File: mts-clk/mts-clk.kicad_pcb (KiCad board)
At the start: 2 copper layers, 70 x 63.6 mm, 71 parts, among them IC1 SCPHS-13.6+, J1 Input (SMA), J2 Output (SMA), J3 Output (SMA), J4 Power Conn., J5 S2B-PH-K-SLFSN, U1 TCP-2-10X, U2 LTC6433BIUF-15-TRPBF, U3 LTC6433BIUF-15-TRPBF, U4 OPA197xD

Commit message: layout for CLK
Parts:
- added G***: LOGO, posm-logo:posm-logo-footprint, F.Cu at (159.4, 132.3)
- moved C27 150.6 mm to (172.9, 121.6)
- moved R11 144.2 mm to (171.1, 125.0), turned to 180 degrees
- moved C28 142.7 mm to (171.2, 114.3)
- moved R12 140.4 mm to (170.2, 121.6), turned to 90 degrees
- moved J3 139.8 mm to (146.4, 131.9)
- moved C25 137.6 mm to (167.4, 101.9), turned to 180 degrees
- moved R13 137.2 mm to (170.2, 117.6), turned to 90 degrees
- moved C26 134.3 mm to (167.4, 99.4), turned to 180 degrees
- moved R14 131.9 mm to (167.7, 113.5)
- moved R16 128.7 mm to (163.4, 109.5), turned to -90 degrees
- moved TP4 127.9 mm to (167.3, 125.6)
- moved R15 127.2 mm to (165.6, 109.5), turned to -90 degrees
- moved L3 124.5 mm to (120.4, 125.2), turned to 180 degrees
- moved C21 121.4 mm to (126.7, 126.8), turned to 90 degrees
- moved TP3 121.1 mm to (164.1, 114.2), turned to 90 degrees
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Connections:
- IC1 pad 12: Net-(IC1-GROUND_10) -> GND
- IC1 pad 13: Net-(IC1-GROUND_10) -> GND
- IC1 pad 14: Net-(IC1-GROUND_10) -> GND
- J3 pad 3: (no net) -> GND
- J3 pad 4: (no net) -> GND
- J3 pad 5: (no net) -> GND
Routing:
- net PORT2: track 0.00 -> 15.1 mm
- net PORT1: track 0.00 -> 13.7 mm
- net 10MHz_EOM: track 0.00 -> 12.5 mm
- net PORT2_POST_amp: track 0.00 -> 10.4 mm
- net 10MHz_DEMOD: track 0.00 -> 10.1 mm
- net Net-(L3-Pad1): track 0.00 -> 7.86 mm
- net Net-(U3-FDBK): track 0.00 -> 7.84 mm, vias 0 -> 2
- net FDBK1: track 0.00 -> 7.59 mm
- net FDBK2: track 0.00 -> 7.30 mm
- net 10MHz_INPUT: track 0.00 -> 6.46 mm
- net Net-(L1-Pad1): track 0.00 -> 5.70 mm
- net PORT1_POST_amp: track 0.00 -> 5.51 mm
- net Net-(U2-IN): track 0.00 -> 5.46 mm
- net Net-(U3-IN): track 0.00 -> 5.01 mm
- net PORT2_post_phase: track 0.00 -> 4.93 mm
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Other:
- board size 70 x 63.6 mm -> 59.9 x 61.7 mm
- board text added: "mts-clk-v0"

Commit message: idek man
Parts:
- moved C32 6.32 mm to (126.8, 89.7), turned to 180 degrees
- moved C31 4.03 mm to (122.5, 90.1), turned to 0 degrees
- moved C27 2.05 mm to (172.9, 119.6)
- moved C14 0.91 mm to (119.6, 117.3)
- moved C29 0.91 mm to (119.3, 115.8)
- moved R14 0.60 mm to (167.2, 113.9), turned to 90 degrees
- moved C19 0.31 mm to (128.3, 117.3), turned to 90 degrees
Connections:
- J2 pad 3: (no net) -> GND
- J2 pad 4: (no net) -> GND
- J2 pad 5: (no net) -> GND
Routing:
- net TDIODE2: track 0.00 -> 46.9 mm, vias 0 -> 2
- net TDIODE1: track 0.00 -> 18.3 mm, vias 0 -> 2
- net GND: track 0.00 -> 15.8 mm, vias 0 -> 92
- net Net-(R15-Pad1): track 0.00 -> 12.6 mm, vias 0 -> 2
- net Net-(U4--): track 0.00 -> 7.04 mm
- net Net-(U4-+): track 0.00 -> 6.15 mm
- net V_FPGA_PWM: track 4.33 -> 9.18 mm
- net Net-(C27-Pad1): track 0.00 -> 4.60 mm
- net Net-(U3-NFILT): track 0.00 -> 1.91 mm
- net Net-(U3-IN): track 5.01 -> 5.67 mm
- net +5V: vias 0 -> 40
- net +15V: vias 0 -> 14
- added copper zone on F.Cu, net +15V
- added copper zone on In2.Cu, net +15V
- added copper zone on F.Cu, net +5V
- added copper zone on In2.Cu, net +5V
- added copper zone on B.Cu, net GND
- added copper zone on F.Cu, net GND
- added copper zone on In1.Cu, net GND
- added copper zone on F.Cu, net V_CONTROL
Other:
- board size 59.9 x 61.7 mm -> 60.2 x 61.7 mm
- copper layers 2 -> 4

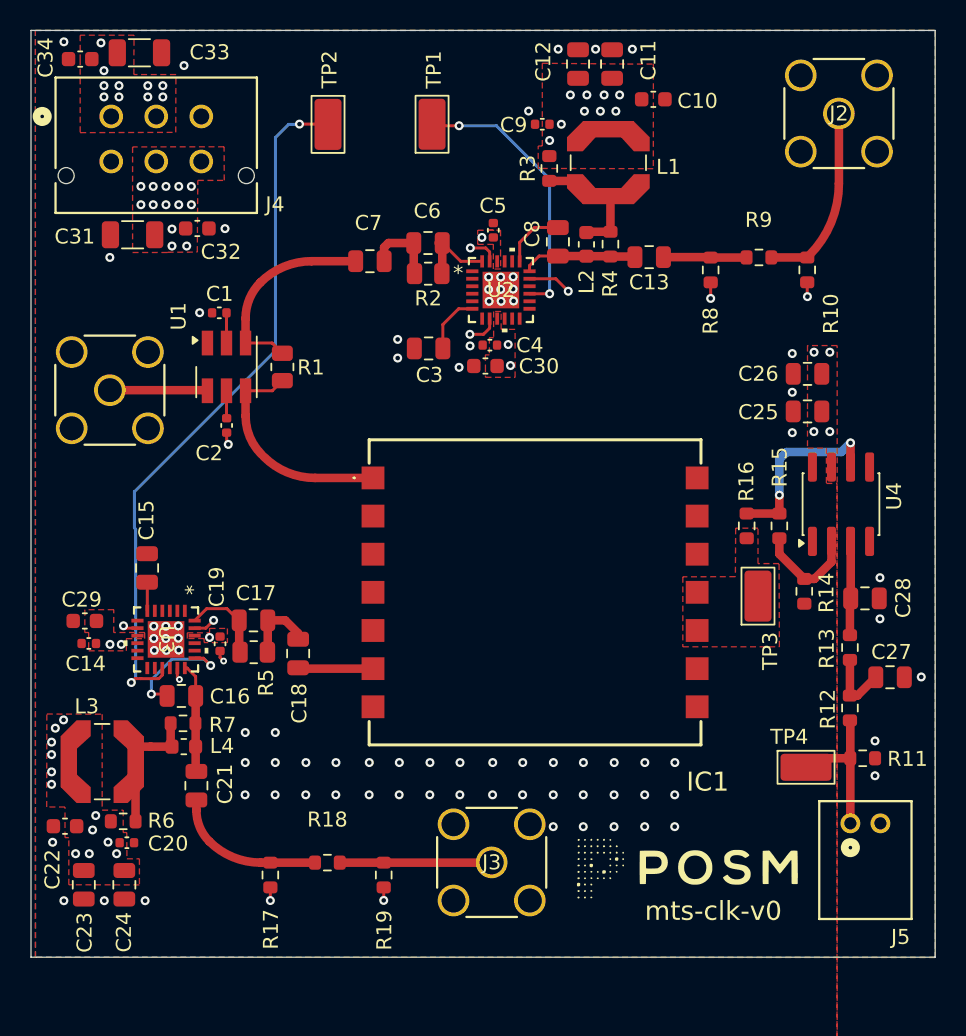
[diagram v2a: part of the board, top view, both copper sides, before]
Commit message: complete with mts-clk v0 layout
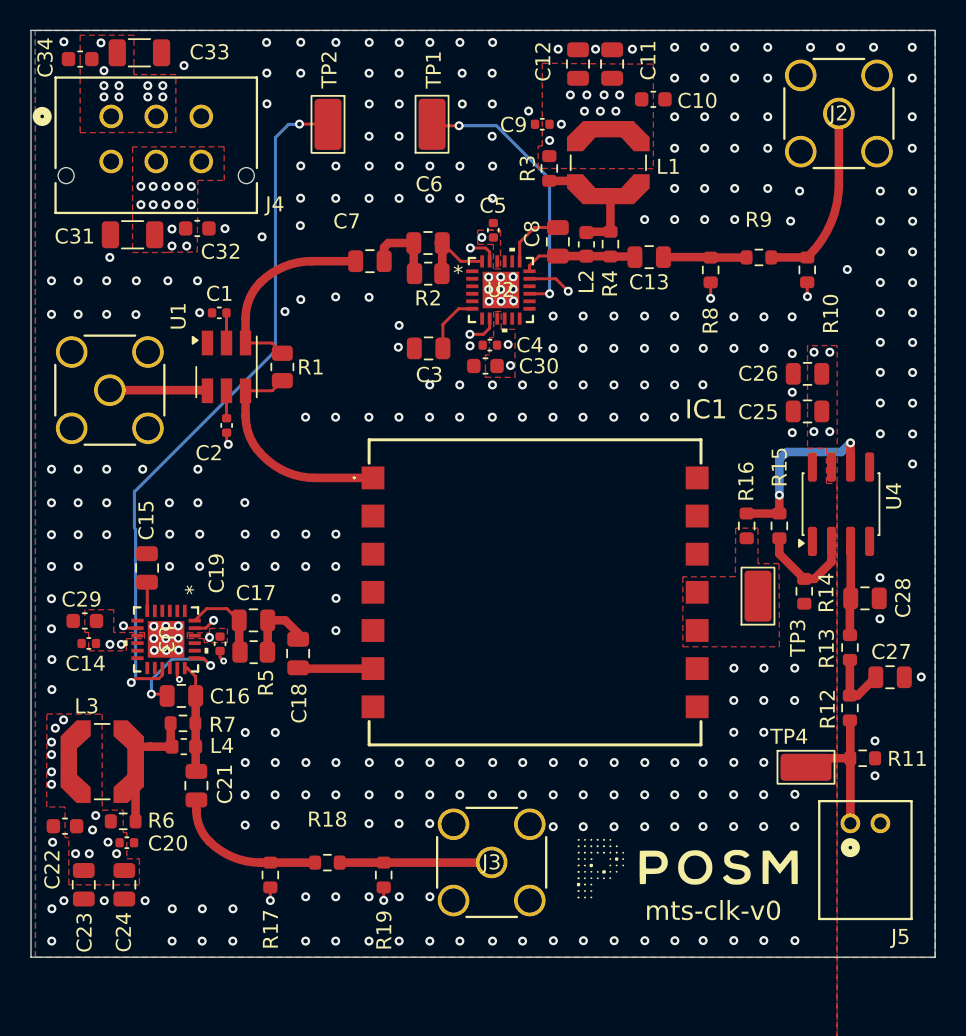
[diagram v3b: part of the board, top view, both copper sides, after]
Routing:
- net GND: vias 92 -> 323

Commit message: final final
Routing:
- net GND: vias 323 -> 305
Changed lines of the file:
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@@
-	)
-	(via
-		(at 158.565 102.26)
-		(size 0.6)
-		(drill 0.3)
-		(layers "F.Cu" "B.Cu")
-		(net "GND")
 	)
 	(via
@@
 	)
 	(via
-		(at 158.575 77.625)
-		(size 0.6)
-		(drill 0.3)
-		(layers "F.Cu" "B.Cu")
-		(net "GND")
-	)
-	(via
 		(at 171.92 126.14)
 		(size 0.6)
@@
 	)
 	(via
-		(at 146.455 85.535)
-		(size 0.6)
-		(drill 0.3)
-		(layers "F.Cu" "B.Cu")
-		(net "GND")
-	)
-	(via
 		(at 166.3 89.2)
 		(size 0.6)
@@
 	)
 	(via
-		(at 158.575 82.25)
-		(size 0.6)
-		(drill 0.3)
-		(layers "F.Cu" "B.Cu")
-		(net "GND")
-	)
-	(via
 		(at 146.435 102.26)
 		(size 0.6)
@@
 	)
 	(via
-		(at 158.575 79.675)
-		(size 0.6)
-		(drill 0.3)
-		(layers "F.Cu" "B.Cu")
-		(net "GND")
-	)
-	(via
-		(at 144.435 81.4)
-		(size 0.6)
-		(drill 0.3)
-		(layers "F.Cu" "B.Cu")
-		(net "GND")
-	)
-	(via
 		(at 144.28 125.26)
 		(size 0.6)
@@
 	)
 	(via
-		(at 146.435 81.4)
-		(size 0.6)
-		(drill 0.3)
-		(layers "F.Cu" "B.Cu")
-		(net "GND")
-	)
-	(via
 		(at 138.235 81.4)
 		(size 0.6)
@@
 	(via
 		(at 117.075 114.35)
-		(size 0.6)
-		(drill 0.3)
-		(layers "F.Cu" "B.Cu")
-		(net "GND")
-	)
-	(via
-		(at 146.445 87.685)
 		(size 0.6)
 		(drill 0.3)
@@
 	)
 	(via
-		(at 158.575 89.1)
-		(size 0.6)
-		(drill 0.3)
-		(layers "F.Cu" "B.Cu")
-		(net "GND")
-	)
-	(via
 		(at 164.515 137.115)
 		(size 0.6)
@@
 	)
 	(via
-		(at 158.575 95.525)
-		(size 0.6)
-		(drill 0.3)
-		(layers "F.Cu" "B.Cu")
-		(net "GND")
-	)
-	(via
 		(at 160.575 87.025)
 		(size 0.6)
@@
 	)
 	(via
-		(at 158.575 84.35)
-		(size 0.6)
-		(drill 0.3)
-		(layers "F.Cu" "B.Cu")
-		(net "GND")
-	)
-	(via
 		(at 136.015 77.3)
 		(size 0.6)
@@
 	)
 	(via
-		(at 118.85 112.2)
-		(size 0.6)
-		(drill 0.3)
-		(layers "F.Cu" "B.Cu")
-		(net "GND")
-	)
-	(via
 		(at 126.95 110.05)
 		(size 0.6)
@@
 	)
 	(via
-		(at 144.275 85.535)
-		(size 0.6)
-		(drill 0.3)
-		(layers "F.Cu" "B.Cu")
-		(net "GND")
-	)
-	(via
 		(at 131.98 125.26)
 		(size 0.6)
@@
 	(via
 		(at 129.98 125.26)
-		(size 0.6)
-		(drill 0.3)
-		(layers "F.Cu" "B.Cu")
-		(net "GND")
-	)
-	(via
-		(at 144.265 87.685)
 		(size 0.6)
 		(drill 0.3)
@@
 	)
 	(via
-		(at 158.575 100.11)
-		(size 0.6)
-		(drill 0.3)
-		(layers "F.Cu" "B.Cu")
-		(net "GND")
-	)
-	(via
 		(at 118.85 105.725)
 		(size 0.6)
@@
 	)
 	(via
+		(at 134.725 97.225)
+		(size 0.6)
+		(drill 0.3)
+		(layers "F.Cu" "B.Cu")
+		(net "GND")
+	)
+	(via
 		(at 152.485 95.525)
 		(size 0.6)
@@
 	)
 	(via
-		(at 155.76 77.75)
-		(size 0.6)
-		(drill 0.3)
-		(layers "F.Cu" "B.Cu")
-		(free yes)
-		(net "GND")
-	)
-	(via
 		(at 151.49 93.87)
 		(size 0.6)
@@
 	)
 	(via
-		(at 146.425 83.55)
-		(size 0.6)
-		(drill 0.3)
-		(layers "F.Cu" "B.Cu")
-		(net "GND")
-	)
-	(via
 		(at 138.22 137.15)
 		(size 0.6)
@@
 	)
 	(via
-		(at 132.625 95.225)
-		(size 0.6)
-		(drill 0.3)
-		(layers "F.Cu" "B.Cu")
-		(net "GND")
-	)
-	(via
-		(at 158.565 97.675)
+		(at 133.125 95.375)
 		(size 0.6)
 		(drill 0.3)
@@
 		(size 0.6)
 		(drill 0.3)
-		(layers "F.Cu" "B.Cu")
-		(net "GND")
-	)
-	(via
-		(at 158.575 87.025)
-		(size 0.6)
-		(drill 0.3)

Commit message: final final final
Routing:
- net GND: vias 305 -> 302
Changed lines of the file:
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@@
-	)
-	(via
-		(at 138.215 102.26)
-		(size 0.6)
-		(drill 0.3)
-		(layers "F.Cu" "B.Cu")
-		(net "GND")
 	)
 	(via
@@
 	)
 	(via
-		(at 135.995 102.26)
-		(size 0.6)
-		(drill 0.3)
-		(layers "F.Cu" "B.Cu")
-		(net "GND")
-	)
-	(via
 		(at 150.475 97.675)
 		(size 0.6)
@@
 		(size 0.6)
 		(drill 0.3)
-		(layers "F.Cu" "B.Cu")
-		(net "GND")
-	)
-	(via
-		(at 133.995 102.26)
-		(size 0.6)
-		(drill 0.3)

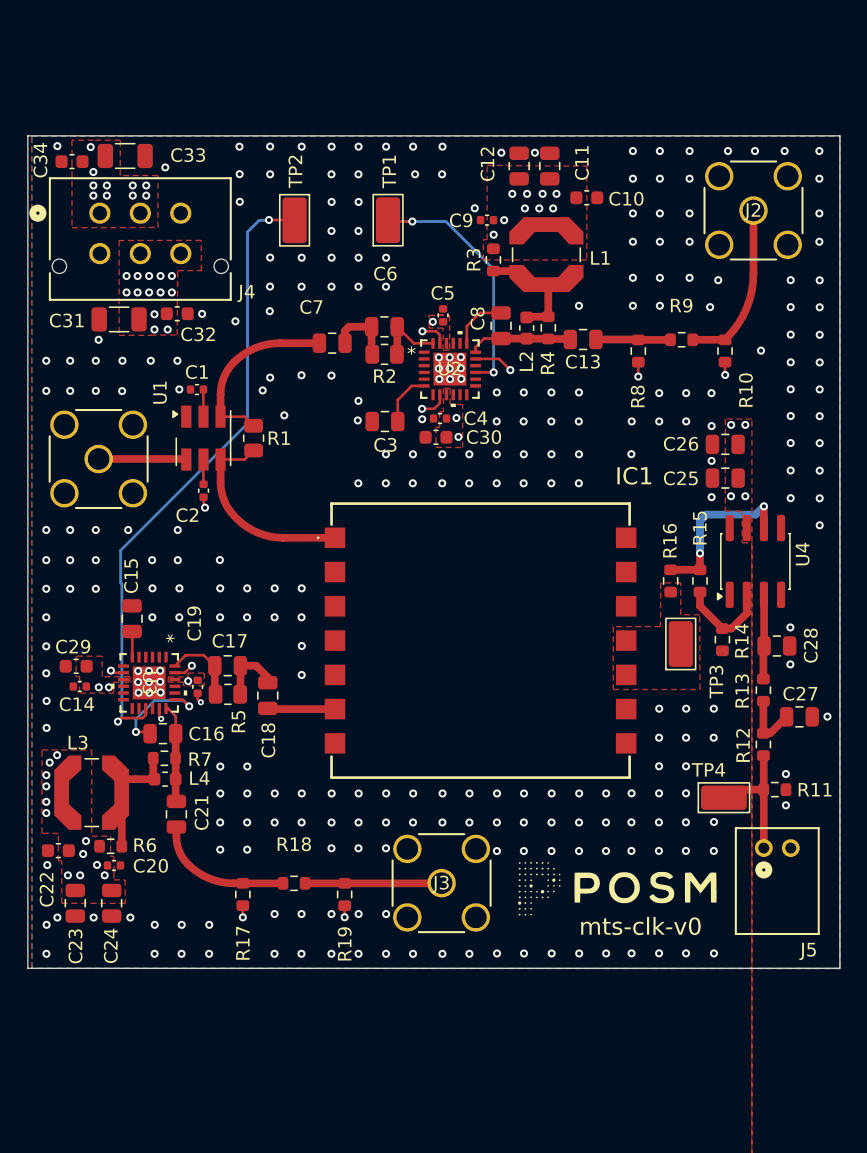
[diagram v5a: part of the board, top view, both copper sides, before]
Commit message: adding mounting holes, more stitching
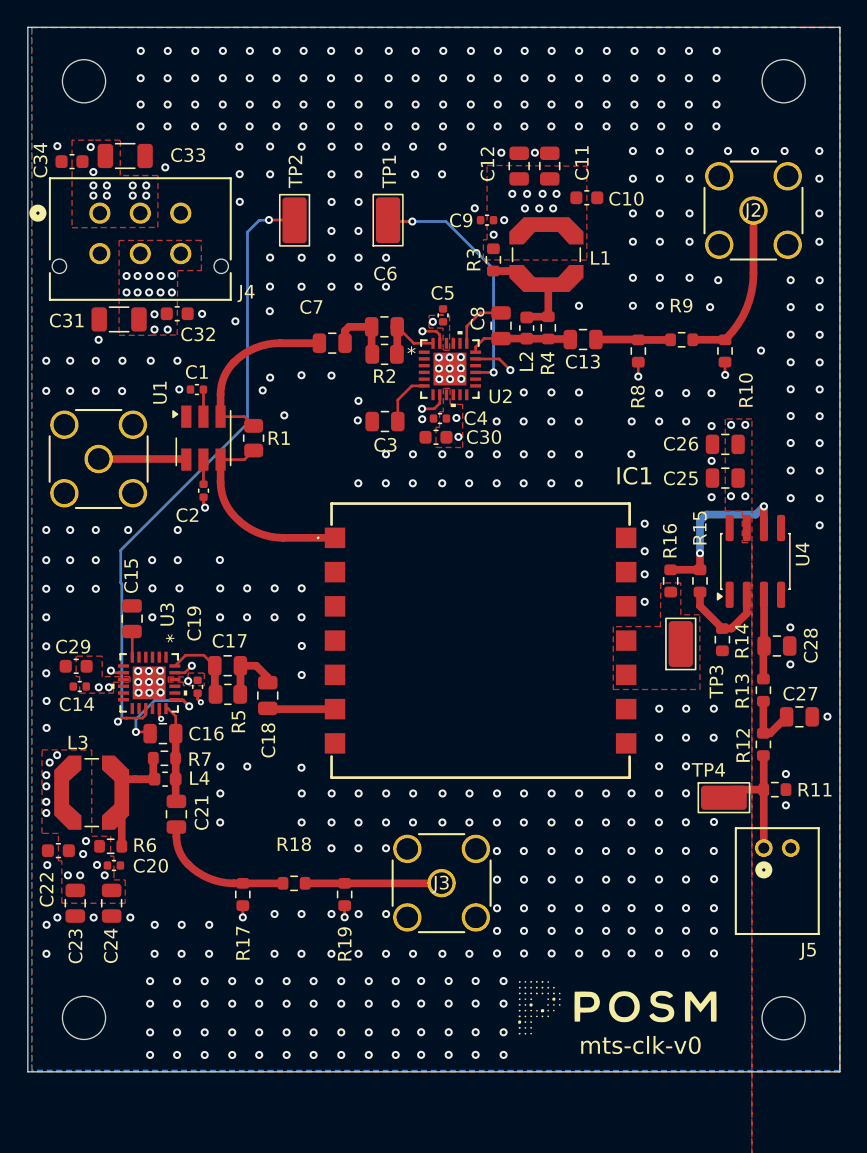
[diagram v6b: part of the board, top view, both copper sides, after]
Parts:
- added REF**: MountingHole_3.2mm_M3, MountingHole:MountingHole_3.2mm_M3, F.Cu at (119.9, 72.5)
- added REF**: MountingHole_3.2mm_M3, MountingHole:MountingHole_3.2mm_M3, F.Cu at (171.8, 141.9)
- added REF**: MountingHole_3.2mm_M3, MountingHole:MountingHole_3.2mm_M3, F.Cu at (119.9, 141.9)
- added REF**: MountingHole_3.2mm_M3, MountingHole:MountingHole_3.2mm_M3, F.Cu at (171.8, 72.5)
- moved G*** 8.83 mm to (159.4, 141.2)
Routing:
- net GND: vias 302 -> 470
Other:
- board size 60.2 x 61.7 mm -> 60.2 x 77.5 mm

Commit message: fixed pour hierarchy
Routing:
- net GND: vias 470 -> 458
- added copper zone on In2.Cu, net GND
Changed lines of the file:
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@@
 	)
 	(via
-		(at 146.455 77.3)
-		(size 0.6)
-		(drill 0.3)
-		(layers "F.Cu" "B.Cu")
-		(net "GND")
-	)
-	(via
 		(at 164.735 70.2)
 		(size 0.6)
@@
 	)
 	(via
-		(at 162.575 79.675)
-		(size 0.6)
-		(drill 0.3)
-		(layers "F.Cu" "B.Cu")
-		(net "GND")
-	)
-	(via
 		(at 160.475 137.115)
 		(size 0.6)
@@
 	)
 	(via
-		(at 162.575 84.35)
-		(size 0.6)
-		(drill 0.3)
-		(layers "F.Cu" "B.Cu")
-		(net "GND")
-	)
-	(via
 		(at 146.45 127.41)
 		(size 0.6)
@@
 	)
 	(via
-		(at 162.575 77.625)
-		(size 0.6)
-		(drill 0.3)
-		(layers "F.Cu" "B.Cu")
-		(net "GND")
-	)
-	(via
 		(at 150.5 131.65)
 		(size 0.6)
@@
 	)
 	(via
-		(at 131.4 77.3)
-		(size 0.6)
-		(drill 0.3)
-		(layers "F.Cu" "B.Cu")
-		(net "GND")
-	)
-	(via
 		(at 166.9 87.2)
 		(size 0.6)
@@
 	)
 	(via
-		(at 162.575 82.25)
-		(size 0.6)
-		(drill 0.3)
-		(layers "F.Cu" "B.Cu")
-		(net "GND")
-	)
-	(via
 		(at 158.59 131.65)
 		(size 0.6)
@@
 	)
 	(via
-		(at 138.235 77.3)
-		(size 0.6)
-		(drill 0.3)
-		(layers "F.Cu" "B.Cu")
-		(net "GND")
-	)
-	(via
 		(at 160.475 135.44)
 		(size 0.6)
@@
 	)
 	(via
-		(at 136.015 77.3)
-		(size 0.6)
-		(drill 0.3)
-		(layers "F.Cu" "B.Cu")
-		(net "GND")
-	)
-	(via
 		(at 158.58 129.53)
 		(size 0.6)
@@
 	)
 	(via
-		(at 144.275 77.3)
-		(size 0.6)
-		(drill 0.3)
-		(layers "F.Cu" "B.Cu")
-		(net "GND")
-	)
-	(via
 		(at 138.225 134.2)
 		(size 0.6)
@@
 	)
 	(via
-		(at 133.675 77.29)
-		(size 0.6)
-		(drill 0.3)
-		(layers "F.Cu" "B.Cu")
-		(net "GND")
-	)
-	(via
 		(at 130.865 144.65)
 		(size 0.6)
@@
 	)
 	(via
-		(at 142.275 77.3)
-		(size 0.6)
-		(drill 0.3)
-		(layers "F.Cu" "B.Cu")
-		(net "GND")
-	)
-	(via
 		(at 164.515 133.76)
 		(size 0.6)
@@
 	)
 	(via
-		(at 140.235 77.3)
-		(size 0.6)
-		(drill 0.3)
-		(layers "F.Cu" "B.Cu")
-		(net "GND")
-	)
-	(via
 		(at 171.825 77.625)
 		(size 0.6)
@@
 		(name "+5V_6")
 		(hatch edge 0.5)
-		(priority 9)
+		(priority 10)
 		(connect_pads yes
 			(clearance 0.5)
@@
 		(name "CONTROL VOLTAGE")
 		(hatch edge 0.5)
-		(priority 15)
+		(priority 16)
 		(connect_pads yes
 			(clearance 0.5)
@@
 		(name "+5V_5")
 		(hatch edge 0.5)
-		(priority 8)
+		(priority 9)
 		(connect_pads yes
 			(clearance 0.2)
@@
 		(name "+5V_4")
 		(hatch edge 0.5)
-		(priority 7)
+		(priority 8)
 		(connect_pads yes
 			(clearance 0.2)
@@
 		(name "+15V")
 		(hatch edge 0.5)
-		(priority 1)
+		(priority 2)
 		(connect_pads yes
 			(clearance 0.5)
@@
 		(name "+5V_2")
 		(hatch edge 0.5)
-		(priority 4)
+		(priority 5)
 		(connect_pads yes
 			(clearance 0.2)
@@
 		(name "+5V")
 		(hatch edge 0.5)
-		(priority 2)
+		(priority 3)
 		(connect_pads yes
 			(clearance 0.5)
@@
 		(name "+5V_3")
 		(hatch edge 0.5)
-		(priority 5)
+		(priority 6)
 		(connect_pads yes
 			(clearance 0.2)
@@
 		(name "+5V_1")
 		(hatch edge 0.5)
-		(priority 3)
+		(priority 4)
 		(connect_pads yes
 			(clearance 0.2)
@@
 		(name "+15V_1")
 		(hatch edge 0.5)
-		(priority 6)
+		(priority 7)
 		(connect_pads yes
 			(clearance 0.5)
@@
 		(name "GND_1")
 		(hatch edge 0.5)
-		(priority 14)
+		(priority 15)
 		(connect_pads yes
 			(clearance 0.5)
@@
 		(name "GND")
 		(hatch edge 0.5)
-		(priority 13)
+		(priority 14)
 		(connect_pads yes
 			(clearance 0.5)
@@
 		(name "+5V_8")
 		(hatch edge 0.5)
-		(priority 12)
+		(priority 13)
 		(connect_pads yes
 			(clearance 0.5)
@@
 		(name "+5V_7")
 		(hatch edge 0.5)
-		(priority 11)
+		(priority 12)
 		(connect_pads yes
 			(clearance 0.5)
@@
 		(name "+15V_2")
 		(hatch edge 0.5)
-		(priority 10)
+		(priority 11)
 		(connect_pads yes
 			(clearance 0.5)
@@
 			)
 		)
+	)
+	(zone
+		(net "GND")
+		(layer "In2.Cu")
+		(hatch edge 0.5)
+		(priority 1)
+		(connect_pads yes
+			(clearance 0.5)
+		)
+		(min_thickness 0.25)
+		(fill yes
+			(thermal_gap 0.5)
+			(thermal_bridge_width 0.5)
+			(island_removal_mode 0)
+		)
+		(polygon
+			(pts
+				(xy 115.725 68.475) (xy 175.925 68.45) (xy 175.925 145.9) (xy 115.725 145.9) (xy 115.7 68.5)
+			)
+		)
